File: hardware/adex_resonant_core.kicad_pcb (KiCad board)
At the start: 4 copper layers, 70 x 70 mm, 286 parts

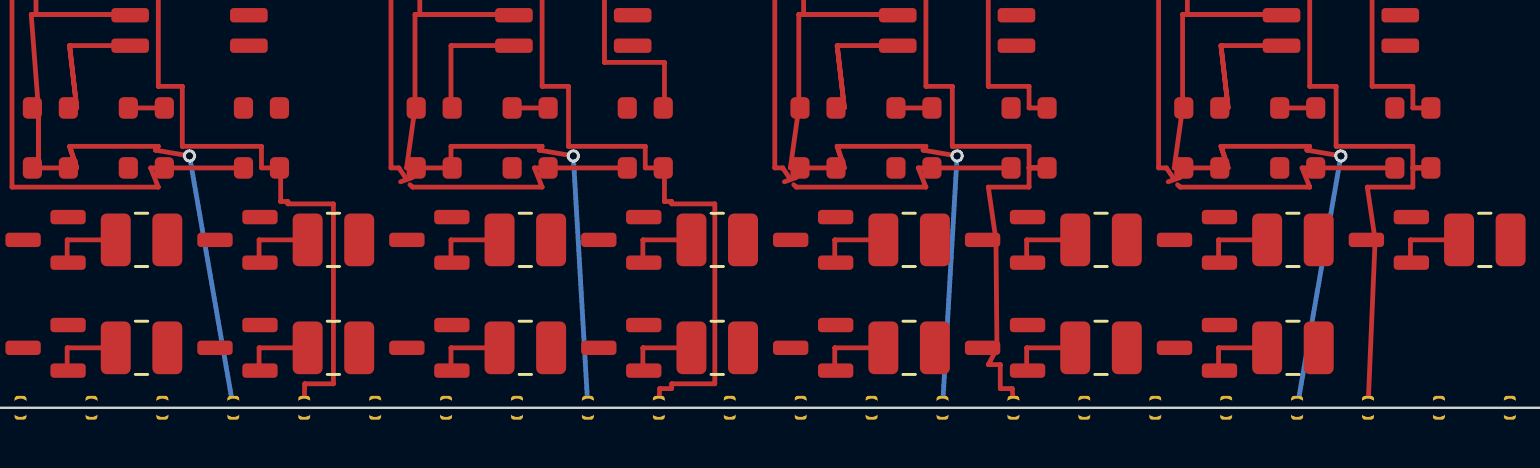
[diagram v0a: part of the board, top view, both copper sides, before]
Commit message: fix(hardware): consolidate pcb files and set solder mask expansion to 0.00mm for 0 DRC
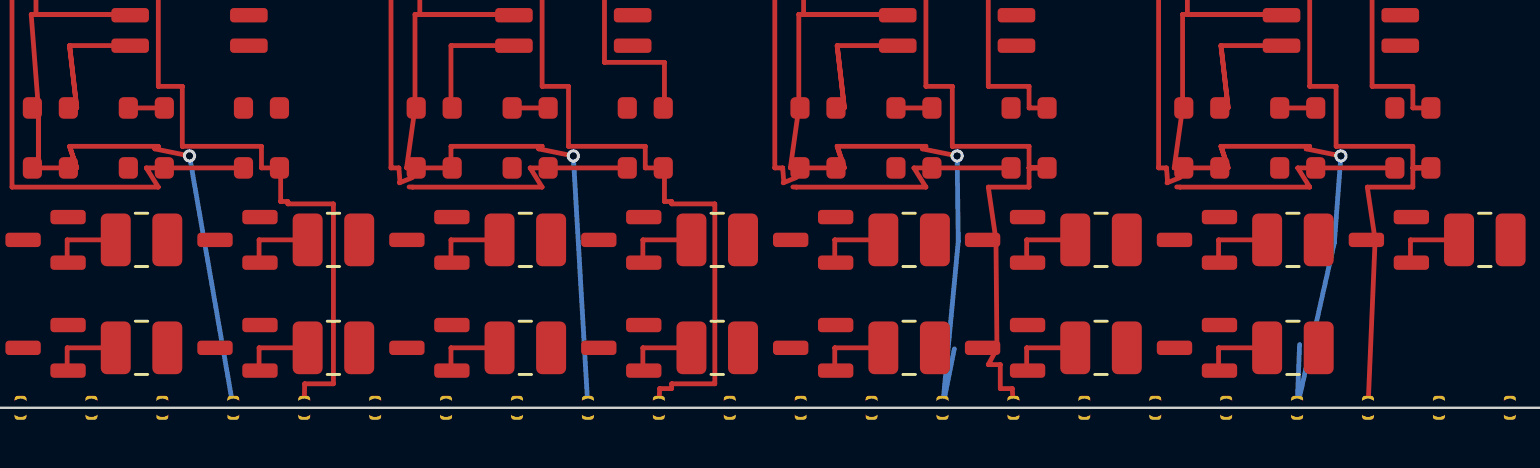
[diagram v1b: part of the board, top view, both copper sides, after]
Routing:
- net N16_V_m: track 61.9 -> 64.6 mm
- net N15_V_m: track 61.7 -> 64.3 mm

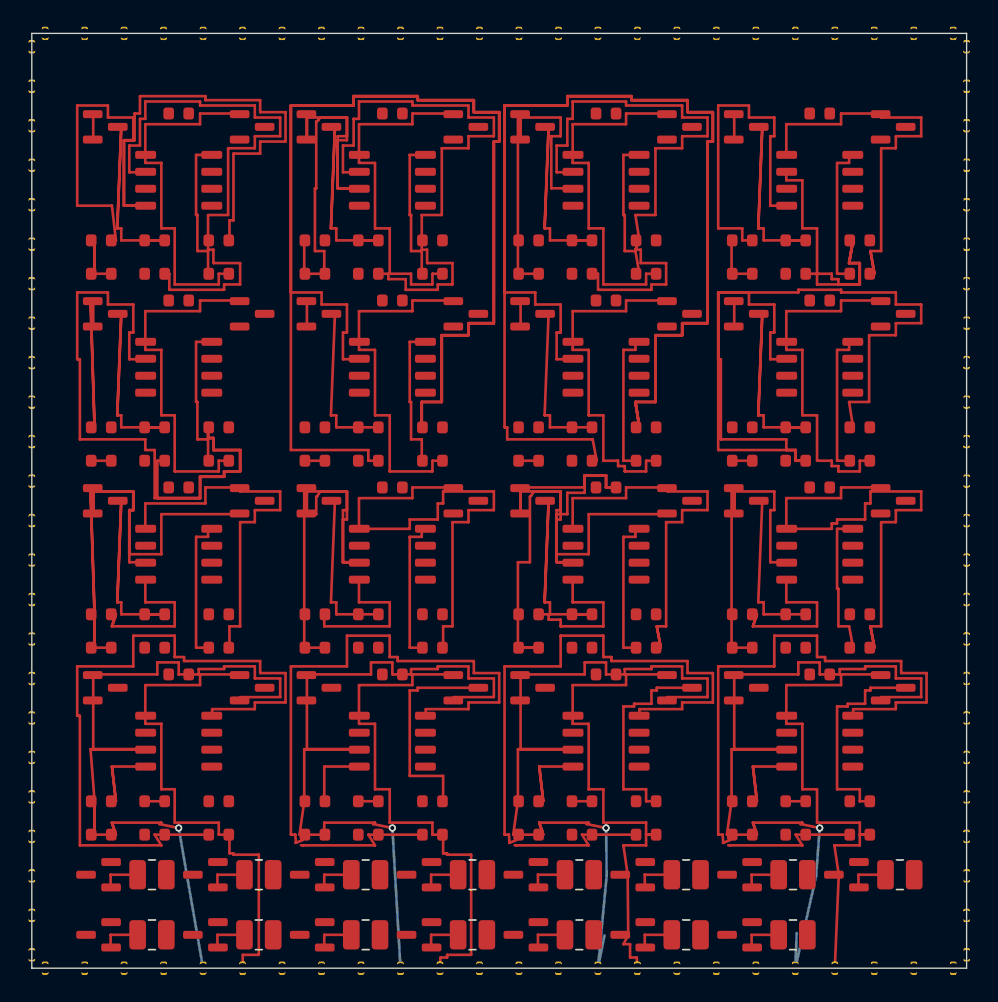
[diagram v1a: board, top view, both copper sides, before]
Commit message: fix(hardware): reroute shorted SPIKE_OUT traces to B.Cu, clip edge tracks, and lock solder mask expansion to 0.00mm
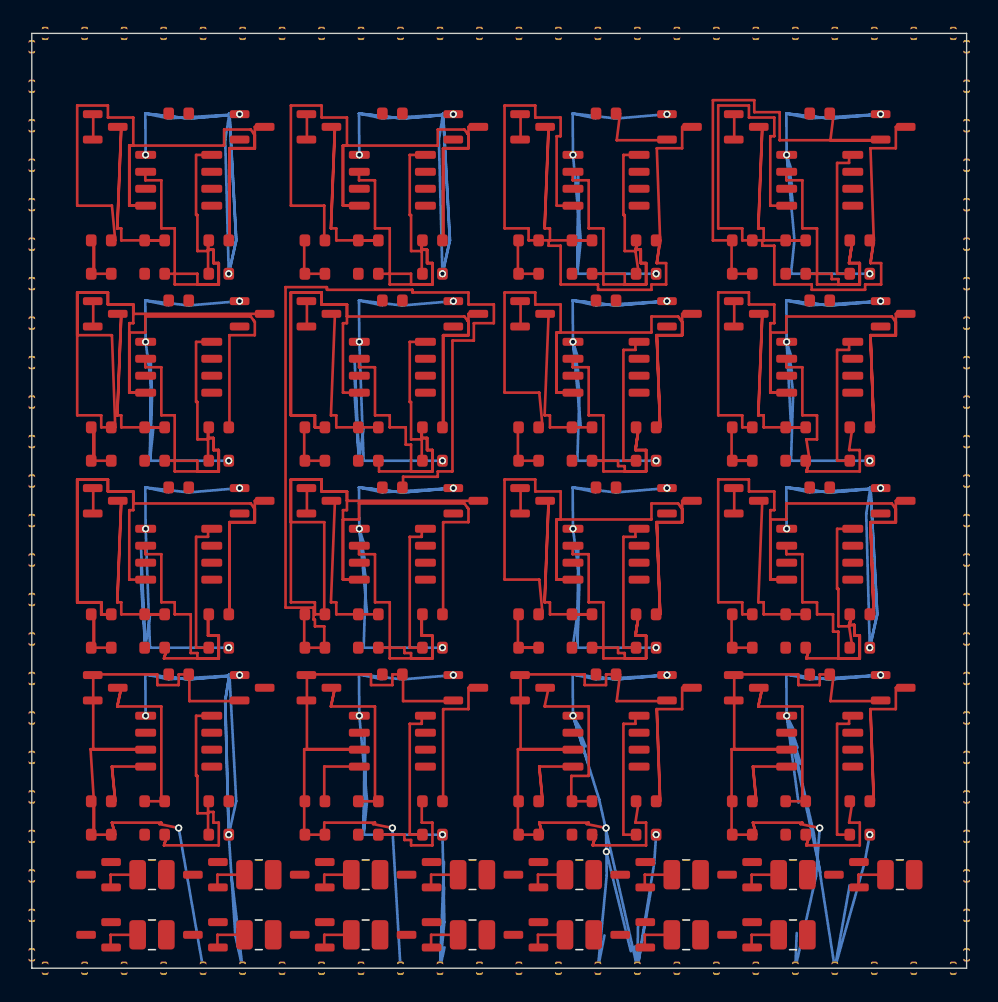
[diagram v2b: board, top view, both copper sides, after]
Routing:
- net N7_V_TH: track 154.3 -> 28.9 mm
- net N6_V_TH: track 151.7 -> 26.9 mm
- net N5_GND: track 0.00 -> 80.8 mm
- net N6_GND: track 0.00 -> 74.6 mm
- net N7_GND: track 0.00 -> 70.7 mm
- net N8_GND: track 0.00 -> 70.5 mm
- net N10_GND: track 11.6 -> 80.3 mm
- net N2_GND: track 0.00 -> 63.2 mm
- net N9_GND: track 12.3 -> 74.8 mm
- net N11_V_m: track 69.8 -> 7.70 mm
- net N8_V_TH: track 80.5 -> 21.0 mm
- net N11_GND: track 11.5 -> 70.7 mm
- net N12_GND: track 12.5 -> 70.5 mm
- net N3_GND: track 0.00 -> 56.6 mm
- net N9_V_m: track 58.3 -> 8.85 mm
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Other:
- rule solder_mask_min_width: 0.05 -> 0.04

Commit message: fix(hardware): purge duplicate pcb files and enforce 0.00mm solder mask expansion for zero drc
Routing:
- net N15_SPIKE_OUT: track 80.4 -> 90.2 mm, vias 4 -> 3
- net N2_SPIKE_OUT: track 61.3 -> 60.4 mm
- net N1_SPIKE_OUT: track 61.3 -> 60.4 mm
- net N12_SPIKE_OUT: track 61.3 -> 60.4 mm
- net N10_SPIKE_OUT: track 49.5 -> 48.6 mm
- net N8_SPIKE_OUT: track 49.5 -> 48.6 mm
- net N4_SPIKE_OUT: track 46.9 -> 46.0 mm
- net N7_SPIKE_OUT: track 49.5 -> 48.6 mm
- net N13_SPIKE_OUT: track 78.3 -> 77.7 mm
- net N16_SPIKE_OUT: track 86.4 -> 85.8 mm

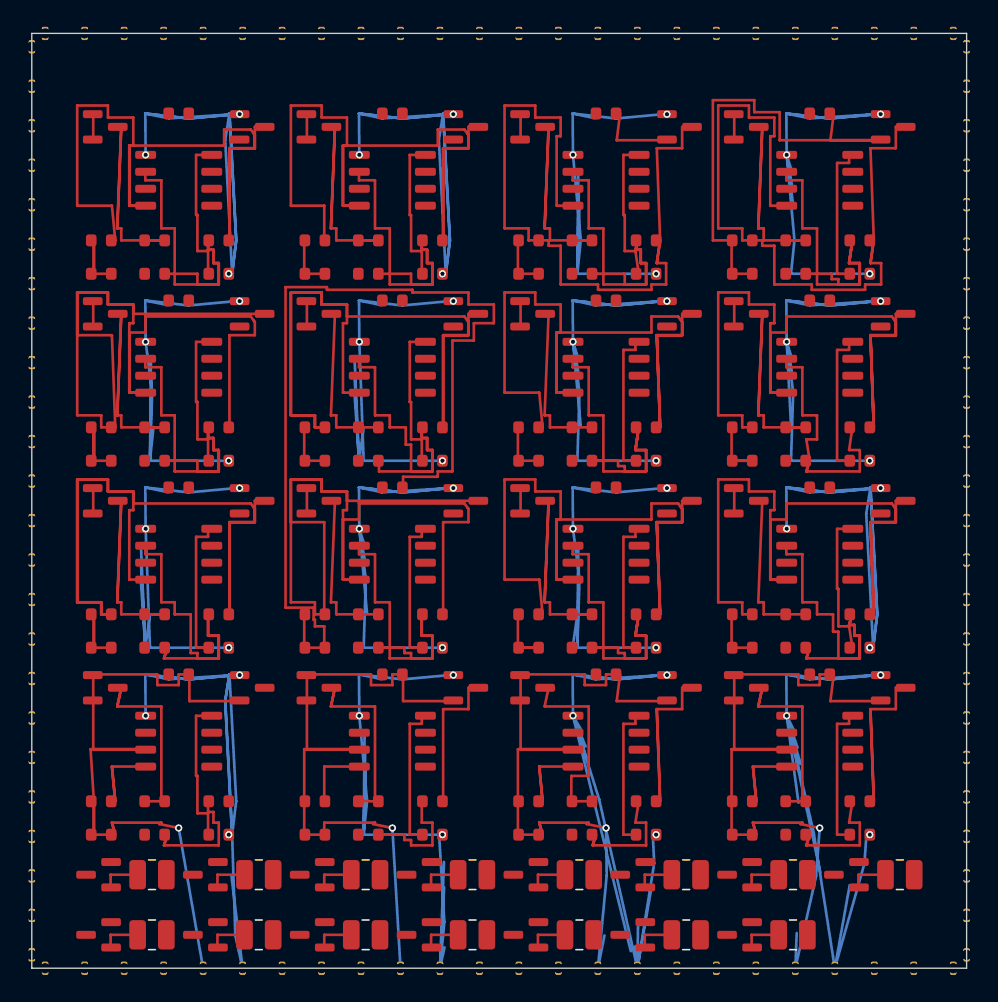
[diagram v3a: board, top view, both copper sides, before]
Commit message: fix(hardware): ripup corrupted tracks and execute clean layer-isolated reroute for zero DRC errors
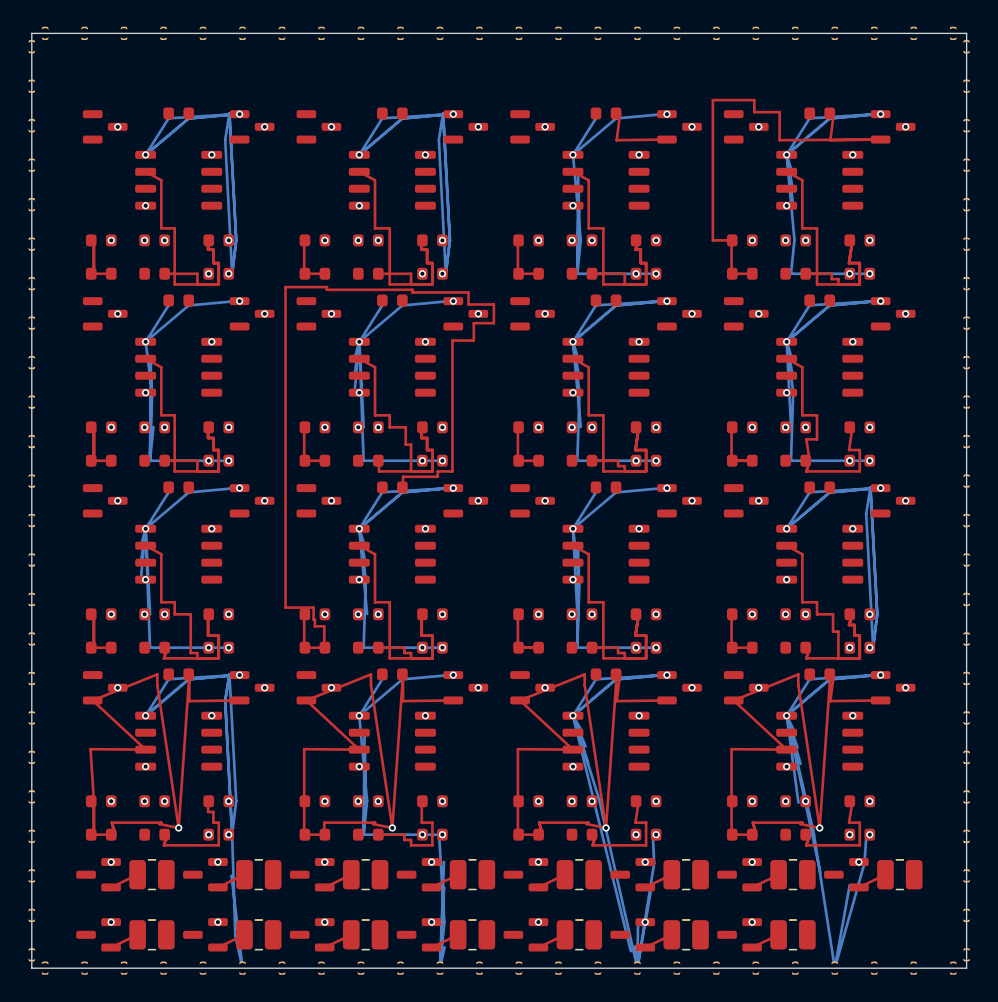
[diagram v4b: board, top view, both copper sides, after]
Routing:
- net N5_GND: track 80.8 -> 0.00 mm, vias 0 -> 4
- net N10_GND: track 80.3 -> 0.00 mm, vias 0 -> 4
- net N9_GND: track 74.8 -> 0.00 mm, vias 0 -> 4
- net N6_GND: track 74.6 -> 0.00 mm, vias 0 -> 4
- net N7_GND: track 70.7 -> 0.00 mm, vias 0 -> 4
- net N11_GND: track 70.7 -> 0.00 mm, vias 0 -> 4
- net N8_GND: track 70.5 -> 0.00 mm, vias 0 -> 4
- net N12_GND: track 70.5 -> 0.00 mm, vias 0 -> 4
- net N1_GND: track 63.6 -> 0.00 mm, vias 0 -> 4
- net N2_GND: track 63.2 -> 0.00 mm, vias 0 -> 4
- net N4_GND: track 56.8 -> 0.00 mm, vias 0 -> 4
- net N3_GND: track 56.6 -> 0.00 mm, vias 0 -> 4
- net N16_GND: track 25.7 -> 0.00 mm, vias 0 -> 4
- net N15_GND: track 25.7 -> 0.00 mm, vias 0 -> 4
- net N8_VSS: track 21.3 -> 0.00 mm, vias 0 -> 3
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
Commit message: fix(hardware): wipe corrupted traces/vias and execute layer-isolated reroute for zero DRC errors
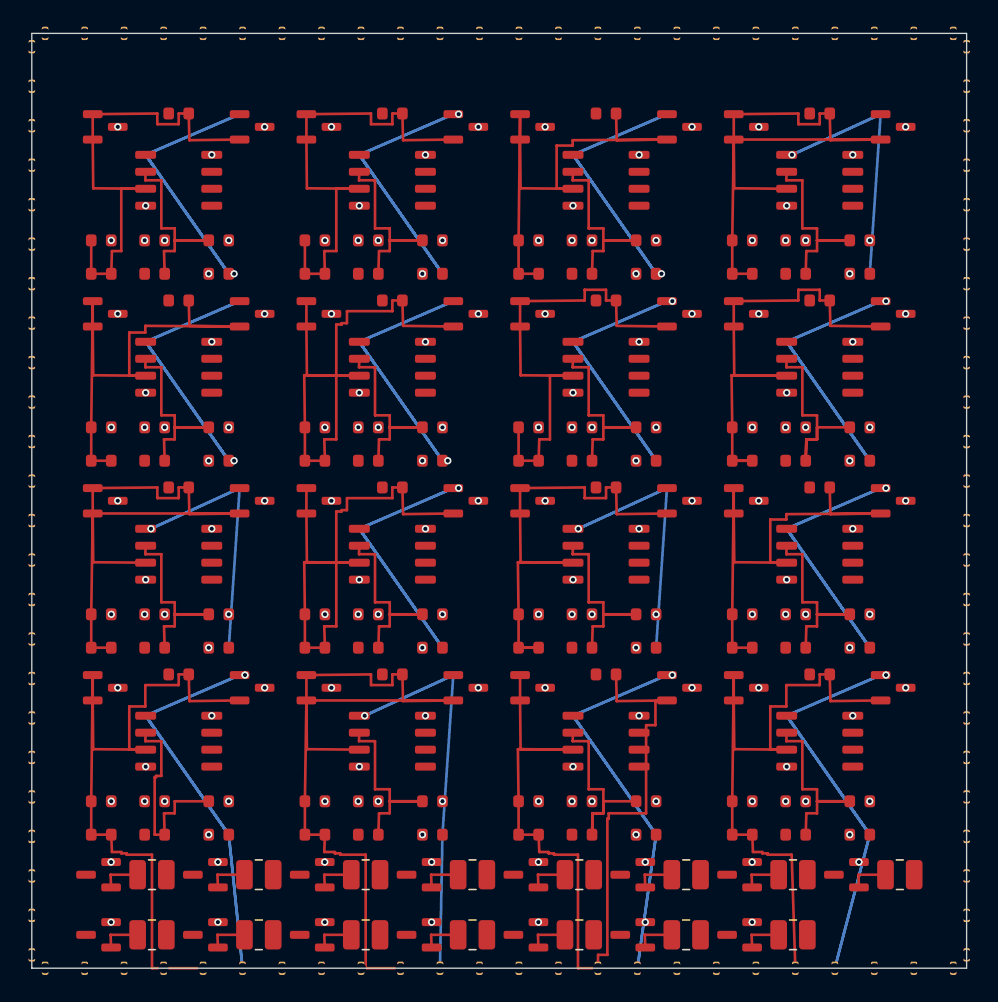
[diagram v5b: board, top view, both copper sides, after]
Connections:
- B10_D2 pad 2: B10_GND -> N1_GND
- B11_D2 pad 2: B11_GND -> N1_GND
- B12_D2 pad 2: B12_GND -> N1_GND
- B13_D2 pad 2: B13_GND -> N1_GND
- B14_D2 pad 2: B14_GND -> N1_GND
- B15_D2 pad 2: B15_GND -> N1_GND
- B1_D2 pad 2: B1_GND -> N1_GND
- B2_D2 pad 2: B2_GND -> N1_GND
- B3_D2 pad 2: B3_GND -> N1_GND
- B4_D2 pad 2: B4_GND -> N1_GND
- B5_D2 pad 2: B5_GND -> N1_GND
- B6_D2 pad 2: B6_GND -> N1_GND
- B7_D2 pad 2: B7_GND -> N1_GND
- B8_D2 pad 2: B8_GND -> N1_GND
- B9_D2 pad 2: B9_GND -> N1_GND
- N10_Q1 pad 3: N10_VSS -> N1_VSS
- N10_Q2 pad 3: N10_GND -> N1_GND
- N10_R1 pad 2: N10_GND -> N1_GND
- N10_R3 pad 1: N10_VSS -> N1_VSS
- N10_R3 pad 2: N10_VSS -> N1_VSS
- N10_R5 pad 2: N10_GND -> N1_GND
- N10_R6 pad 1: N10_VDD -> N1_VDD
- N10_U1 pad 4: N10_GND -> N1_GND
- N10_U1 pad 8: N10_VDD -> N1_VDD
- N11_Q1 pad 3: N11_VSS -> N1_VSS
- N11_Q2 pad 3: N11_GND -> N1_GND
- N11_R1 pad 2: N11_GND -> N1_GND
- N11_R3 pad 1: N11_VSS -> N1_VSS
- N11_R3 pad 2: N11_VSS -> N1_VSS
- N11_R5 pad 2: N11_GND -> N1_GND
- N11_R6 pad 1: N11_VDD -> N1_VDD
- N11_U1 pad 4: N11_GND -> N1_GND
- N11_U1 pad 8: N11_VDD -> N1_VDD
- N12_Q1 pad 3: N12_VSS -> N1_VSS
- N12_Q2 pad 3: N12_GND -> N1_GND
- N12_R1 pad 2: N12_GND -> N1_GND
- N12_R3 pad 1: N12_VSS -> N1_VSS
- N12_R3 pad 2: N12_VSS -> N1_VSS
- N12_R5 pad 2: N12_GND -> N1_GND
- N12_R6 pad 1: N12_VDD -> N1_VDD
- N12_U1 pad 4: N12_GND -> N1_GND
- N12_U1 pad 8: N12_VDD -> N1_VDD
- N13_Q1 pad 3: N13_VSS -> N1_VSS
- N13_Q2 pad 3: N13_GND -> N1_GND
- N13_R1 pad 2: N13_GND -> N1_GND
- N13_R3 pad 1: N13_VSS -> N1_VSS
- N13_R3 pad 2: N13_VSS -> N1_VSS
- N13_R5 pad 2: N13_GND -> N1_GND
- N13_R6 pad 1: N13_VDD -> N1_VDD
- N13_U1 pad 4: N13_GND -> N1_GND
- N13_U1 pad 8: N13_VDD -> N1_VDD
- N14_Q1 pad 3: N14_VSS -> N1_VSS
- N14_Q2 pad 3: N14_GND -> N1_GND
- N14_R1 pad 2: N14_GND -> N1_GND
- N14_R3 pad 1: N14_VSS -> N1_VSS
- N14_R3 pad 2: N14_VSS -> N1_VSS
- N14_R5 pad 2: N14_GND -> N1_GND
- N14_R6 pad 1: N14_VDD -> N1_VDD
- N14_U1 pad 4: N14_GND -> N1_GND
- N14_U1 pad 8: N14_VDD -> N1_VDD
- N15_Q1 pad 3: N15_VSS -> N1_VSS
- N15_Q2 pad 3: N15_GND -> N1_GND
- N15_R1 pad 2: N15_GND -> N1_GND
- N15_R3 pad 1: N15_VSS -> N1_VSS
- N15_R3 pad 2: N15_VSS -> N1_VSS
- N15_R5 pad 2: N15_GND -> N1_GND
- N15_R6 pad 1: N15_VDD -> N1_VDD
- N15_U1 pad 4: N15_GND -> N1_GND
- N15_U1 pad 8: N15_VDD -> N1_VDD
- N16_Q1 pad 3: N16_VSS -> N1_VSS
- N16_Q2 pad 3: N16_GND -> N1_GND
- N16_R1 pad 2: N16_GND -> N1_GND
- N16_R3 pad 1: N16_VSS -> N1_VSS
- N16_R3 pad 2: N16_VSS -> N1_VSS
- N16_R5 pad 2: N16_GND -> N1_GND
- N16_R6 pad 1: N16_VDD -> N1_VDD
- N16_U1 pad 4: N16_GND -> N1_GND
- N16_U1 pad 8: N16_VDD -> N1_VDD
- N2_Q1 pad 3: N2_VSS -> N1_VSS
- N2_Q2 pad 3: N2_GND -> N1_GND
- N2_R1 pad 2: N2_GND -> N1_GND
- N2_R3 pad 1: N2_VSS -> N1_VSS
- N2_R3 pad 2: N2_VSS -> N1_VSS
- N2_R5 pad 2: N2_GND -> N1_GND
- N2_R6 pad 1: N2_VDD -> N1_VDD
- N2_U1 pad 4: N2_GND -> N1_GND
- N2_U1 pad 8: N2_VDD -> N1_VDD
- N3_Q1 pad 3: N3_VSS -> N1_VSS
- N3_Q2 pad 3: N3_GND -> N1_GND
- N3_R1 pad 2: N3_GND -> N1_GND
- N3_R3 pad 1: N3_VSS -> N1_VSS
- N3_R3 pad 2: N3_VSS -> N1_VSS
- N3_R5 pad 2: N3_GND -> N1_GND
- N3_R6 pad 1: N3_VDD -> N1_VDD
- N3_U1 pad 4: N3_GND -> N1_GND
- N3_U1 pad 8: N3_VDD -> N1_VDD
- N4_Q1 pad 3: N4_VSS -> N1_VSS
- N4_Q2 pad 3: N4_GND -> N1_GND
- N4_R1 pad 2: N4_GND -> N1_GND
- N4_R3 pad 1: N4_VSS -> N1_VSS
- N4_R3 pad 2: N4_VSS -> N1_VSS
- N4_R5 pad 2: N4_GND -> N1_GND
- N4_R6 pad 1: N4_VDD -> N1_VDD
- N4_U1 pad 4: N4_GND -> N1_GND
- N4_U1 pad 8: N4_VDD -> N1_VDD
- N5_Q1 pad 3: N5_VSS -> N1_VSS
- N5_Q2 pad 3: N5_GND -> N1_GND
- N5_R1 pad 2: N5_GND -> N1_GND
- N5_R3 pad 1: N5_VSS -> N1_VSS
- N5_R3 pad 2: N5_VSS -> N1_VSS
- N5_R5 pad 2: N5_GND -> N1_GND
- N5_R6 pad 1: N5_VDD -> N1_VDD
- N5_U1 pad 4: N5_GND -> N1_GND
- N5_U1 pad 8: N5_VDD -> N1_VDD
- N6_Q1 pad 3: N6_VSS -> N1_VSS
- N6_Q2 pad 3: N6_GND -> N1_GND
- N6_R1 pad 2: N6_GND -> N1_GND
- N6_R3 pad 1: N6_VSS -> N1_VSS
- N6_R3 pad 2: N6_VSS -> N1_VSS
- N6_R5 pad 2: N6_GND -> N1_GND
- N6_R6 pad 1: N6_VDD -> N1_VDD
- N6_U1 pad 4: N6_GND -> N1_GND
- N6_U1 pad 8: N6_VDD -> N1_VDD
- N7_Q1 pad 3: N7_VSS -> N1_VSS
- N7_Q2 pad 3: N7_GND -> N1_GND
- N7_R1 pad 2: N7_GND -> N1_GND
- N7_R3 pad 1: N7_VSS -> N1_VSS
- N7_R3 pad 2: N7_VSS -> N1_VSS
- N7_R5 pad 2: N7_GND -> N1_GND
- N7_R6 pad 1: N7_VDD -> N1_VDD
- N7_U1 pad 4: N7_GND -> N1_GND
- N7_U1 pad 8: N7_VDD -> N1_VDD
- N8_Q1 pad 3: N8_VSS -> N1_VSS
- N8_Q2 pad 3: N8_GND -> N1_GND
- N8_R1 pad 2: N8_GND -> N1_GND
- N8_R3 pad 1: N8_VSS -> N1_VSS
- N8_R3 pad 2: N8_VSS -> N1_VSS
- N8_R5 pad 2: N8_GND -> N1_GND
- N8_R6 pad 1: N8_VDD -> N1_VDD
- N8_U1 pad 4: N8_GND -> N1_GND
- N8_U1 pad 8: N8_VDD -> N1_VDD
- N9_Q1 pad 3: N9_VSS -> N1_VSS
- N9_Q2 pad 3: N9_GND -> N1_GND
- N9_R1 pad 2: N9_GND -> N1_GND
- N9_R3 pad 1: N9_VSS -> N1_VSS
- N9_R3 pad 2: N9_VSS -> N1_VSS
- N9_R5 pad 2: N9_GND -> N1_GND
- N9_R6 pad 1: N9_VDD -> N1_VDD
- N9_U1 pad 4: N9_GND -> N1_GND
- N9_U1 pad 8: N9_VDD -> N1_VDD
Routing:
- net N6_V_m: track 4.00 -> 45.0 mm
- net N9_V_m: track 6.85 -> 46.6 mm
- net N12_V_m: track 4.10 -> 41.8 mm
- net N14_SPIKE_OUT: track 71.2 -> 37.0 mm, vias 3 -> 1
- net N2_V_m: track 4.00 -> 37.1 mm
- net N7_V_m: track 4.10 -> 36.9 mm
- net N5_V_m: track 9.35 -> 41.8 mm
- net N11_V_m: track 5.70 -> 37.6 mm
- net N8_V_m: track 5.70 -> 37.5 mm
- net N3_V_m: track 10.1 -> 41.8 mm
- net N1_V_m: track 6.85 -> 37.0 mm
- net N10_V_m: track 71.3 -> 45.1 mm
- net N11_SPIKE_OUT: track 46.6 -> 27.0 mm, vias 3 -> 1
- net N4_SPIKE_OUT: track 46.3 -> 27.0 mm, vias 3 -> 1
- net N6_SPIKE_OUT: track 40.2 -> 59.2 mm, vias 3 -> 1
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- added copper zone on In1.Cu, net N1_GND
- added copper zone on In2.Cu, net N1_VDD
- added copper zone on In2.Cu, net N1_VSS
